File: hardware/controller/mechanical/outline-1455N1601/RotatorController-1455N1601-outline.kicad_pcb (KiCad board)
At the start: 4 copper layers, 159 x 99 mm, 3 parts

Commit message: Generate enclosure machining drawings from the layout.
Panel sheets no longer live on the outline board. A script reads
Panel, PanelCutout, and PanelZ from footprints and writes 1:1 plate
drawings, including the top-wall drills from the triac bar.

Co-authored-by: Jeffrey Millar <wa1hco@users.noreply.github.com>
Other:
- board text removed: "BRAKE D4.0"
- board text removed: "CCW BTN D6.5"
- board text removed: "CCW D4.0"
- board text removed: "CW BTN D6.5"
- board text removed: "CW D4.0"
- board text removed: "DATUM"
- board text removed: "FAULT D4.0"
- board text removed: "FRONT PANEL - Hammond 1455N1601 end plate, VIEWED FROM OUTSIDE"
- board text removed: "GND STUD D4.3 TBD"
- board text removed: "LINK D4.0"
- board text removed: "Old V4 panel drawings (70x99 board, 35x76 panels, light pipes LP4-EP, Az preset pot) are superseded by these."
- board text removed: "POWER IN 22.00x12.50 TBD"
- board text removed: "PWR D4.0"
- board text removed: "REAR PANEL - Hammond 1455N1601 end plate, VIEWED FROM OUTSIDE"
- board text removed: "RJ45 17.02x14.60"
- board text removed: "ROTOR GLAND D16.3 TBD"
- board text removed: "STOP BTN D6.5"
- board text removed: "USB-C 13.60x6.50"
- board text removed: "datum (0,0) = lower-left corner; PCB top face at Y=27.40 (slot 6)"

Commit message: Record the AC version's single 26 VAC feed and rotor-return ground.
Logic power is half-wave rectified from that feed, then a non-isolated buck and an LDO. The rear-panel Powerpole default is a pigtail gland; the bracket cutout stays TBD.

Co-authored-by: Jeffrey Millar <wa1hco@users.noreply.github.com>
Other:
- board text added: "26 VAC PP z+11.00 gland; bracket TBD"
- board text added: "REAR: rotor cable, 26 VAC Powerpoles, USB-C, RJ45"
- board text removed: "POWER IN z+6.00"
- board text removed: "REAR: rotor cable, 13.8 V, 26 VAC, USB-C, RJ45"
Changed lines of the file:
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@@
 		)
 	)
-	(gr_text "POWER IN z+6.00"
+	(gr_text "26 VAC PP z+11.00 gland; bracket TBD"
 		(at 48 65.5 0)
 		(layer "Cmts.User")
@@
 		)
 	)
-	(gr_text "REAR: rotor cable, 13.8 V, 26 VAC, USB-C, RJ45"
+	(gr_text "REAR: rotor cable, 26 VAC Powerpoles, USB-C, RJ45"
 		(at 39.9 99.5 90)
 		(layer "Cmts.User")

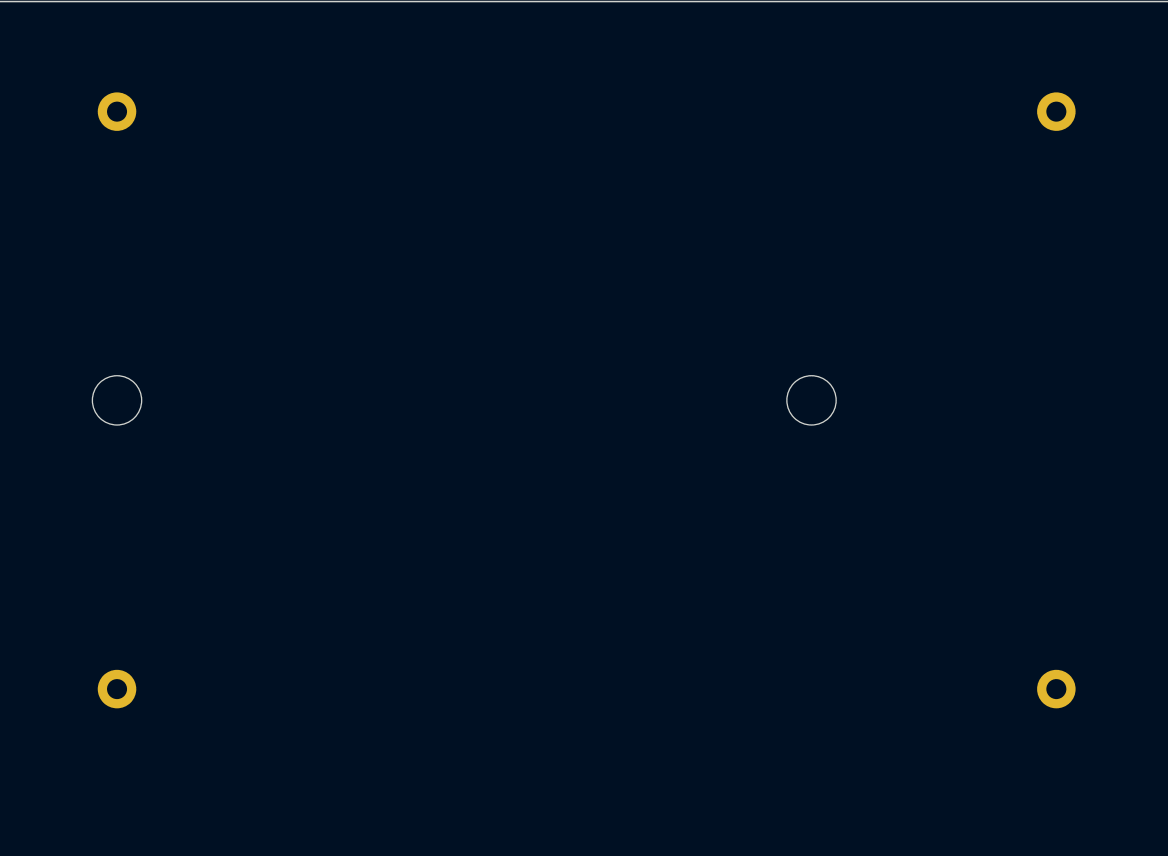
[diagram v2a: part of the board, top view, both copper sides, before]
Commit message: Move the outline motor-run caps to the bottom side.
The top of the Hammond slot-6 board is crowded, so C_MOTOR1 and C_MOTOR2 hang below the board. The heat bar stays on top. Both footprints move to B.Cu, fab and courtyard move to B.Fab and B.CrtYd, and the flat-cap lead bend reverses up into the board. A +3.6 mm shift in +y keeps the 20.3 mm body outside the 8.5 mm bottom-edge strip and the corner bosses.

Co-authored-by: Jeffrey Millar <wa1hco@users.noreply.github.com>
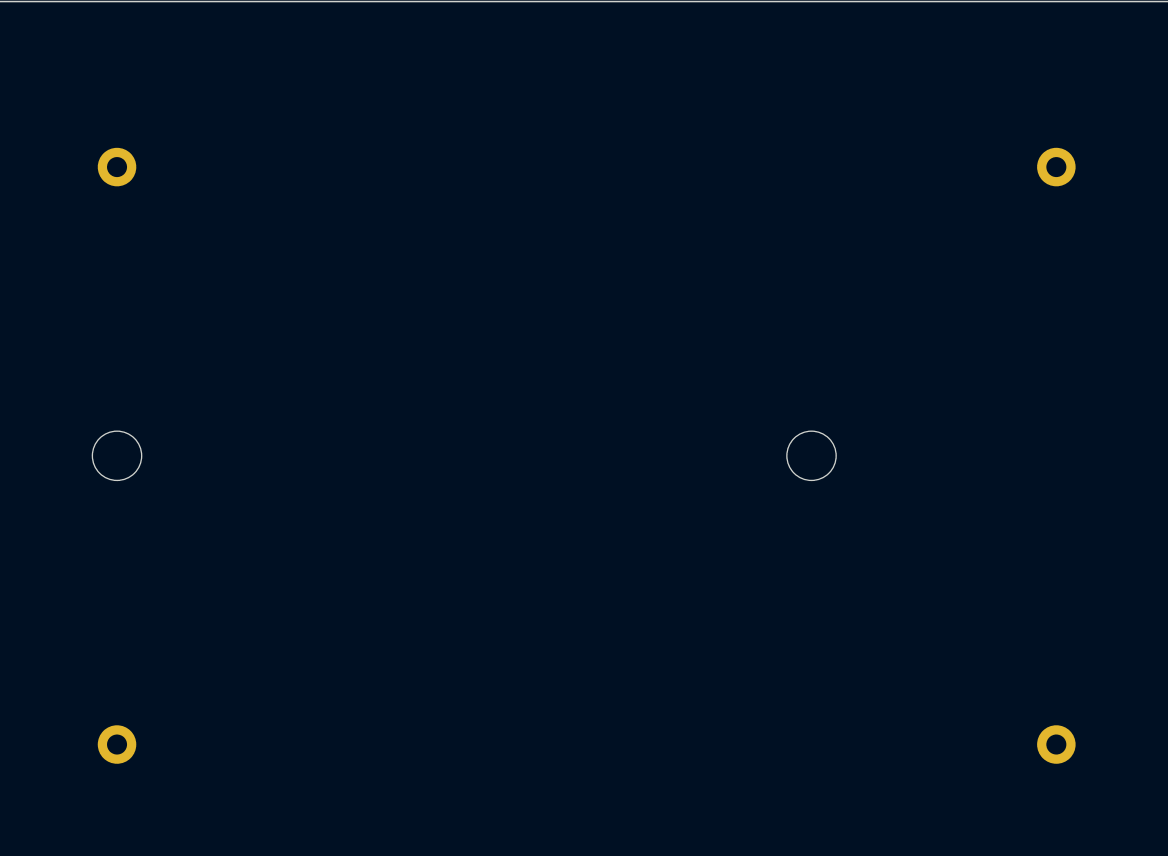
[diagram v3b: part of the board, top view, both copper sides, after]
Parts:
- C_MOTOR1, C_MOTOR2: moved to B.Cu
- moved C_MOTOR1 3.60 mm to (99.0, 60.8)
- moved C_MOTOR2 3.60 mm to (160.0, 60.8)
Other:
- board text added: "BOTTOM (6 mm leads: seat on the board, solder from the top)"
- board text added: "BOTTOM C_MOTOR1 R60EW61005000K 100uF flat, H 20.3"
- board text added: "BOTTOM C_MOTOR2"
- board text added: "BOTTOM, UPRIGHT, H 15.0 max"
- board text added: "BOTTOM. 41.5x40 face on board; leads exit 41.5x20 face at ~10.2 below PCB,"
- board text added: "BOTTOM: C_MOTOR1 || C_MOTOR2 = 133 uF (CDE 130-156); pad 1-1, 2-2"
- board text added: "BOTTOM: cable tie (2.5 mm) through 2x NPTH 3.2 around the body, or RTV it to the board"
- board text added: "BOTTOM: leads straight up through the board (solder from the top)"
- board text added: "BOTTOM: run 2.5 outboard then bend 90 deg up into the board (r ~1, >=1 mm straight from body)"
- board text removed: "(6 mm leads: no flat mount)"
- board text removed: "41.5x40 face on board; leads exit 41.5x20 face at ~10.2 above PCB,"
- board text removed: "C_MOTOR1 R60EW61005000K 100uF flat, H 20.3"
- board text removed: "C_MOTOR1 || C_MOTOR2 = 133 uF (CDE 130-156); pad 1-1, 2-2"
- board text removed: "C_MOTOR2"
- board text removed: "UPRIGHT, H 15.0 max"
- board text removed: "cable tie (2.5 mm) through 2x NPTH 3.2 over body, or RTV the body down"
- board text removed: "leads 1.0 straight down"
- board text removed: "run 2.5 outboard then bend 90 deg down (r ~1, >=1 mm straight from body)"
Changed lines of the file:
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@@
 	)
 	(footprint "C_Rect_KEMET_R60_P37.5_L41.5_W20_H40_Flat"
-		(layer "F.Cu")
-		(at 99 57.15)
+		(layer "B.Cu")
+		(at 99 60.75)
 		(property "Reference" "C_MOTOR1"
 			(at 0 0 0)
-			(layer "F.SilkS")
+			(layer "B.SilkS")
 			(hide yes)
 			(effects
@@
 		(property "Value" "R60EW61005000K"
 			(at 0 0 0)
-			(layer "F.Fab")
+			(layer "B.Fab")
 			(hide yes)
 			(effects
@@
 		(property "Datasheet" ""
 			(at 0 0 0)
-			(layer "F.Fab")
+			(layer "B.Fab")
 			(hide yes)
 			(effects
@@
 		(property "Description" ""
 			(at 0 0 0)
-			(layer "F.Fab")
+			(layer "B.Fab")
 			(hide yes)
 			(effects
@@
 	)
 	(footprint "C_Rect_TDK_B32526T_P37.5_L41.5_W24_H15_Upright"
-		(layer "F.Cu")
-		(at 160 57.15)
+		(layer "B.Cu")
+		(at 160 60.75)
 		(property "Reference" "C_MOTOR2"
 			(at 0 0 0)
-			(layer "F.SilkS")
+			(layer "B.SilkS")
 			(hide yes)
 			(effects
@@
 		(property "Value" "B32526T1336K000"
 			(at 0 0 0)
-			(layer "F.Fab")
+			(layer "B.Fab")
 			(hide yes)
 			(effects
@@
 		(property "Datasheet" ""
 			(at 0 0 0)
-			(layer "F.Fab")
+			(layer "B.Fab")
 			(hide yes)
 			(effects
@@
 		(property "Description" ""
 			(at 0 0 0)
-			(layer "F.Fab")
+			(layer "B.Fab")
 			(hide yes)
 			(effects
@@
 	)
 	(gr_rect
-		(start 148 55.15)
-		(end 172 96.65)
+		(start 148 58.75)
+		(end 172 100.25)
 		(stroke
 			(width 0.1)
@@
 	)
 	(gr_rect
-		(start 101.5 55)
-		(end 141.6 96.8)
+		(start 101.5 58.6)
+		(end 141.6 100.4)
 		(stroke
 			(width 0.1)
@@
 	)
 	(gr_rect
-		(start 97.25 54.5)
-		(end 146.2 97.3)
+		(start 97.25 58.1)
+		(end 146.2 100.9)
 		(stroke
 			(width 0.05)
@@
 		)
 		(fill no)
-		(layer "F.CrtYd")
+		(layer "B.CrtYd")
 	)
 	(gr_rect
-		(start 147.5 54.65)
-		(end 172.5 97.15)
+		(start 147.5 58.25)
+		(end 172.5 100.75)
 		(stroke
 			(width 0.05)
@@
 		)
 		(fill no)
-		(layer "F.CrtYd")
+		(layer "B.CrtYd")
 	)
 	(gr_rect
@@
 	)
 	(gr_line
-		(start 101.5 94.65)
-		(end 99 94.65)
+		(start 101.5 98.25)
+		(end 99 98.25)
 		(stroke
 			(width 0.3)
 			(type default)
 		)
-		(layer "F.Fab")
+		(layer "B.Fab")
 	)
 	(gr_line
-		(start 101.5 57.15)
-		(end 99 57.15)
+		(start 101.5 60.75)
+		(end 99 60.75)
 		(stroke
 			(width 0.3)
 			(type default)
 		)
-		(layer "F.Fab")
+		(layer "B.Fab")
 	)
 	(gr_circle
@@
 	)
 	(gr_rect
-		(start 148 55.15)
-		(end 172 96.65)
+		(start 148 58.75)
+		(end 172 100.25)
 		(stroke
 			(width 0.15)
@@
 		)
 		(fill no)
-		(layer "F.Fab")
+		(layer "B.Fab")
 	)
 	(gr_rect
-		(start 101.5 55)
-		(end 141.6 96.8)
+		(start 101.5 58.6)
+		(end 141.6 100.4)
 		(stroke
 			(width 0.15)
@@
 		)
 		(fill no)
-		(layer "F.Fab")
+		(layer "B.Fab")
 	)
 	(gr_line
-		(start 99 75.9)
-		(end 144.1 75.9)
+		(start 99 79.5)
+		(end 144.1 79.5)
 		(stroke
 			(width 0.08)
 			(type default)
 		)
-		(layer "F.Fab")
+		(layer "B.Fab")
 	)
 	(gr_circle
@@
 	)
 	(gr_text "AC motor side 26-30 VAC (cap rated 63 VAC); >=15 mm from bar"
-		(at 121.55 80.3 0)
+		(at 121.55 83.9 0)
 		(layer "Cmts.User")
 		(effects
@@
 		)
 	)
-	(gr_text "(6 mm leads: no flat mount)"
-		(at 160 81.9 0)
+	(gr_text "BOTTOM (6 mm leads: seat on the board, solder from the top)"
+		(at 160 85.5 0)
 		(layer "Cmts.User")
 		(effects
@@
 		)
 	)
-	(gr_text "C_MOTOR1 || C_MOTOR2 = 133 uF (CDE 130-156); pad 1-1, 2-2"
-		(at 121.55 82.3 0)
+	(gr_text "BOTTOM: C_MOTOR1 || C_MOTOR2 = 133 uF (CDE 130-156); pad 1-1, 2-2"
+		(at 121.55 85.9 0)
 		(layer "Cmts.User")
 		(effects
@@
 	)
 	(gr_text "33uF 100VDC/63VAC"
-		(at 160 73.9 0)
+		(at 160 77.5 0)
 		(layer "Cmts.User")
 		(effects
@@
 		)
 	)
-	(gr_text "run 2.5 outboard then bend 90 deg down (r ~1, >=1 mm straight from body)"
-		(at 121.55 76.1 0)
+	(gr_text "BOTTOM: run 2.5 outboard then bend 90 deg up into the board (r ~1, >=1 mm straight from body)"
+		(at 121.55 79.7 0)
 		(layer "Cmts.User")
 		(effects
@@
 		)
 	)
-	(gr_text "41.5x40 face on board; leads exit 41.5x20 face at ~10.2 above PCB,"
-		(at 121.55 74.3 0)
+	(gr_text "BOTTOM. 41.5x40 face on board; leads exit 41.5x20 face at ~10.2 below PCB,"
+		(at 121.55 77.9 0)
 		(layer "Cmts.User")
 		(effects
@@
 		)
 	)
-	(gr_text "leads 1.0 straight down"
-		(at 160 79.9 0)
+	(gr_text "BOTTOM: leads straight up through the board (solder from the top)"
+		(at 160 83.5 0)
 		(layer "Cmts.User")
 		(effects
@@
 		)
 	)
-	(gr_text "cable tie (2.5 mm) through 2x NPTH 3.2 over body, or RTV the body down"
-		(at 121.55 78.3 0)
+	(gr_text "BOTTOM: cable tie (2.5 mm) through 2x NPTH 3.2 around the body, or RTV it to the board"
+		(at 121.55 81.9 0)
 		(layer "Cmts.User")
 		(effects
@@
 	)
 	(gr_text "24 x 41.5 footprint"
-		(at 160 77.9 0)
+		(at 160 81.5 0)
 		(layer "Cmts.User")
 		(effects
@@
 	)
 	(gr_text "RTV dot at base optional"
-		(at 160 83.9 0)
+		(at 160 87.5 0)
 		(layer "Cmts.User")
 		(effects
@@
 		)
 	)
-	(gr_text "UPRIGHT, H 15.0 max"
-		(at 160 75.9 0)
+	(gr_text "BOTTOM, UPRIGHT, H 15.0 max"
+		(at 160 79.5 0)
 		(layer "Cmts.User")
 		(effects
@@
 		)
 	)
-	(gr_text "C_MOTOR2"
-		(at 160 69.9 0)
-		(layer "F.Fab")
+	(gr_text "BOTTOM C_MOTOR2"
+		(at 160 73.5 0)
+		(layer "B.Fab")
 		(effects
 			(font
@@
 				(thickness 0.18)
 			)
+			(justify mirror)
 		)
 	)
-	(gr_text "C_MOTOR1 R60EW61005000K 100uF flat, H 20.3"
-		(at 121.55 71.9 0)
-		(layer "F.Fab")
+	(gr_text "BOTTOM C_MOTOR1 R60EW61005000K 100uF flat, H 20.3"
+		(at 121.55 75.5 0)
+		(layer "B.Fab")
 		(effects
 			(font
@@
 				(thickness 0.18)
 			)
+			(justify mirror)
 		)
 	)
 	(gr_text "B32526T1336K000"
-		(at 160 71.9 0)
-		(layer "F.Fab")
+		(at 160 75.5 0)
+		(layer "B.Fab")
 		(effects
 			(font
@@
 				(thickness 0.165)
 			)
+			(justify mirror)
 		)
 	)
@@
 		(layer "Dwgs.User")
 		(pts
-			(xy 103 57.15) (xy 103 94.65)
+			(xy 103 60.75) (xy 103 98.25)
 		)
 		(height 0)
@@
 		)
 		(gr_text "37.50 mm"
-			(at 101.65 75.9 90)
+			(at 101.65 79.5 90)
 			(layer "Dwgs.User")
 			(effects
@@
 		(layer "Dwgs.User")
 		(pts
-			(xy 101.5 96.8) (xy 141.6 96.8)
+			(xy 101.5 100.4) (xy 141.6 100.4)
 		)
 		(height -7)
@@
 		)
 		(gr_text "40.10 mm"
-			(at 121.55 88.45 0)
+			(at 121.55 92.05 0)
 			(layer "Dwgs.User")
 			(effects
@@
 		(layer "Dwgs.User")
 		(pts
-			(xy 148 96.65) (xy 172 96.65)
+			(xy 148 100.25) (xy 172 100.25)
 		)
 		(height -7)
@@
 		)
 		(gr_text "24.00 mm"
-			(at 160 88.3 0)
+			(at 160 91.9 0)
 			(layer "Dwgs.User")
 			(effects
@@
 		(layer "Dwgs.User")
 		(pts
-			(xy 141.6 99.65) (xy 148 99.65)
+			(xy 141.6 103.25) (xy 148 103.25)
 		)
 		(height 0)
@@
 		)
 		(gr_text "6.40 mm"
-			(at 144.8 98.3 0)
+			(at 144.8 101.9 0)
 			(layer "Dwgs.User")
 			(effects
@@
 		(layer "Dwgs.User")
 		(pts
-			(xy 172 55.15) (xy 172 96.65)
+			(xy 172 58.75) (xy 172 100.25)
 		)
 		(height -5)
@@
 		)
 		(gr_text "41.50 mm"
-			(at 175.65 75.9 90)
+			(at 175.65 79.5 90)
 			(layer "Dwgs.User")
 			(effects
@@
 		(layer "Dwgs.User")
 		(pts
-			(xy 50 57) (xy 99 57)
+			(xy 50 60.6) (xy 99 60.6)
 		)
 		(height 0)
@@
 		)
 		(gr_text "49.00 mm"
-			(at 74.5 55.65 0)
+			(at 74.5 59.25 0)
 			(layer "Dwgs.User")
 			(effects
@@
 		(layer "Dwgs.User")
 		(pts
-			(xy 141.6 55) (xy 141.6 96.8)
+			(xy 141.6 58.6) (xy 141.6 100.4)
 		)
 		(height -6)
@@
 		)
 		(gr_text "41.80 mm"
-			(at 146.25 75.9 90)
+			(at 146.25 79.5 90)
 			(layer "Dwgs.User")
 			(effects
@@
 		(layer "Dwgs.User")
 		(pts
-			(xy 99 96.8) (xy 101.5 96.8)
+			(xy 99 100.4) (xy 101.5 100.4)
 		)
 		(height -4)
@@
 		)
 		(gr_text "2.50 mm"
-			(at 100.25 91.45 0)
+			(at 100.25 95.05 0)
 			(layer "Dwgs.User")
 			(effects
@@
 		(layer "Dwgs.User")
 		(pts
-			(xy 163 57.15) (xy 163 94.65)
+			(xy 163 60.75) (xy 163 98.25)
 		)
 		(height 0)
@@
 		)
 		(gr_text "37.50 mm"
-			(at 161.65 75.9 90)
+			(at 161.65 79.5 90)
 			(layer "Dwgs.User")
 			(effects
